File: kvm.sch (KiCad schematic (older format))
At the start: 35 parts, among them J1 USB_C_Receptacle, J2 Conn_ARM_JTAG_SWD_10, J3 USB_C_Receptacle, J4 USB_C_Receptacle, SW1 SW_Push, U1 MAX17501AxTB, U2 HD3SS3212, U3 HD3SS3212, U4 HD3SS3212, U5 STM32F030F4Px, U6 TS3A5223RSW, U7 UCS3205, U8 TS3A5223RSW, U9 UCS3205, Y1 16MHz

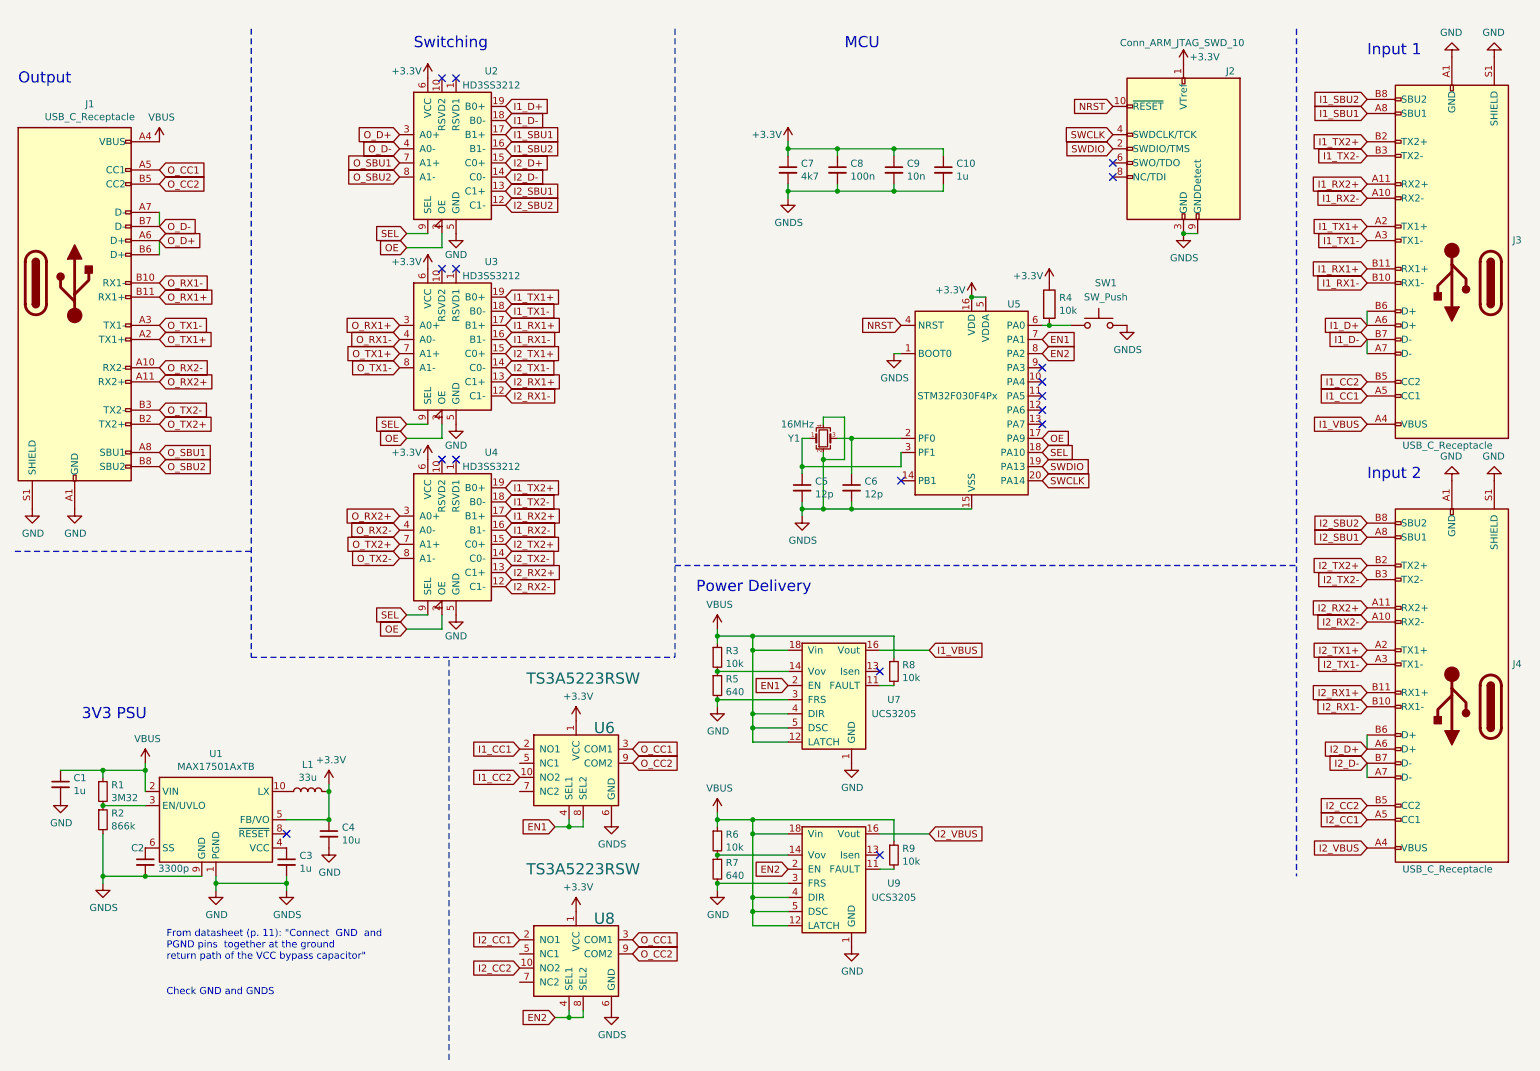
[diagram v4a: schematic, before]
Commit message: Fixed errors in component schematics and added decoupling caps
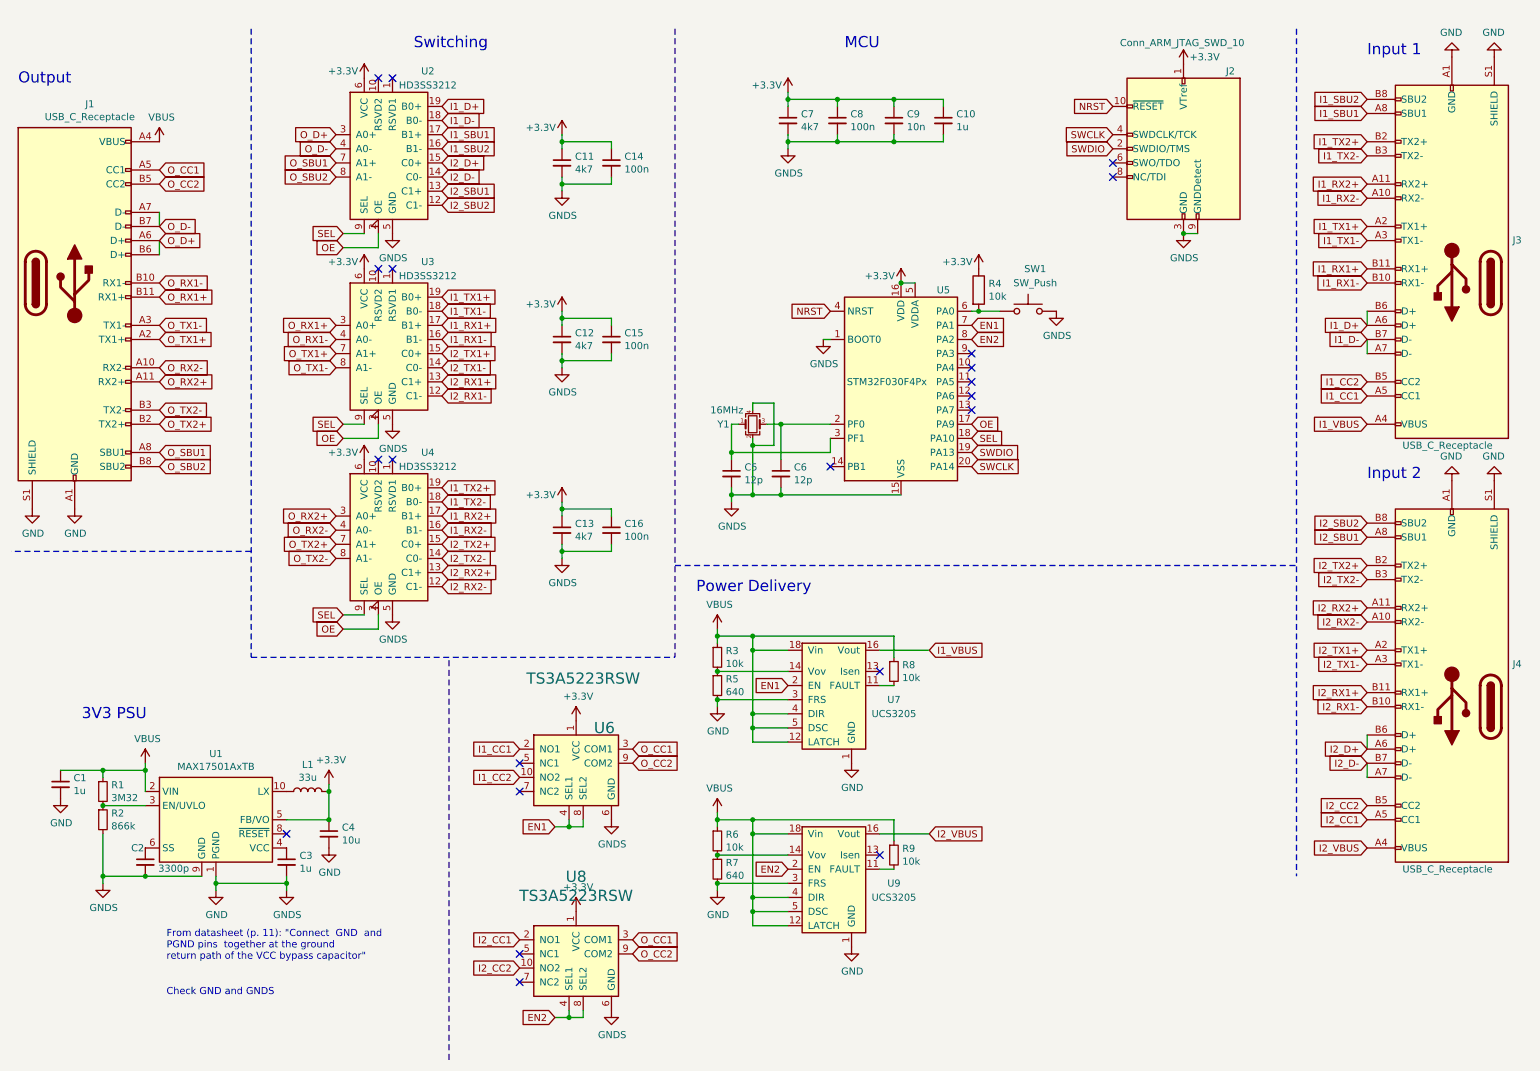
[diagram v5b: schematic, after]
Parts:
- added C11, C12, C13: 4k7, Capacitor_SMD:C_0402_1005Metric, symbol Device:C_Small
- added C14, C15, C16: 100n, Capacitor_SMD:C_0402_1005Metric, symbol Device:C_Small
- C1, C2, C3, C4: footprint (none) -> Capacitor_SMD:C_1206_3216Metric
- C10, C5, C6, C7, C8, C9: footprint (none) -> Capacitor_SMD:C_0402_1005Metric
- R1, R2, R3, R5, R6, R7, R8, R9: footprint (none) -> Resistor_SMD:R_1206_3216Metric
- R4: footprint Resistor_SMD:R_0805_2012Metric -> Resistor_SMD:R_0402_1005Metric
- U6, U8: footprint (none) -> VQFN20:VQFN19_3x3x0.9mm
- Y1: footprint (none) -> Crystal:Crystal_SMD_SeikoEpson_TSX3225-4Pin_3.2x2.5mm
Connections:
- net +3V3: now also C11.1, C12.1, C13.1, C14.1, C15.1, C16.1
- net GND: now also C11.2, C12.2, C13.2, C14.2, C15.2, C16.2
- no-connect marks 17 -> 21
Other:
- moved on the sheet: C10, C5, C6, C7, C8, C9, R4, SW1, U2, U3, U4, U5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

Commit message: Added separate power input for control circuit
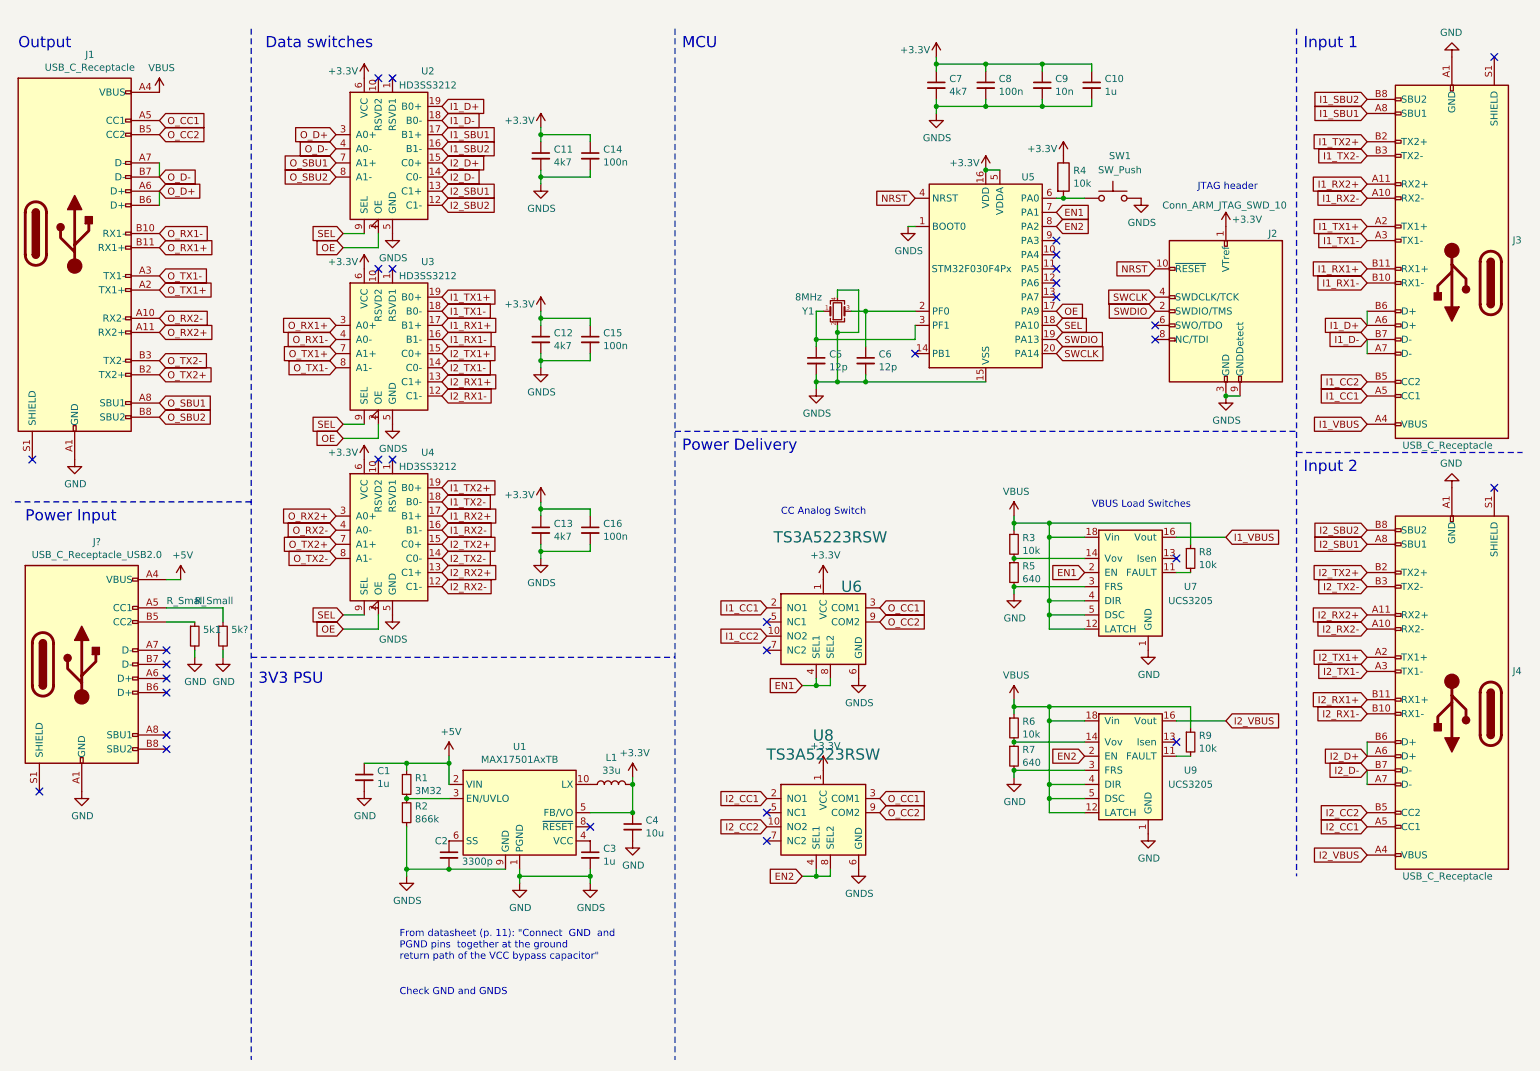
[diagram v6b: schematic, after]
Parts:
- added 5k1, 5k?: R_Small, symbol Device:R_Small
- added J?: USB_C_Receptacle_USB2.0, symbol Connector:USB_C_Receptacle_USB2.0
- Y1: value 16MHz -> 8MHz
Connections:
- net GND: now also 5k1.2, 5k?.2, J?.A1 (GND), J?.A12 (GND), J?.B1 (GND), J?.B12 (GND); no longer J1.S1 (SHIELD), J3.S1 (SHIELD), J4.S1 (SHIELD)
- net VBUS: no longer C1.1, R1.1, U1.2 (VIN)
- new net: 5k?.1, J?.A5 (CC1)
- new net: 5k1.1, J?.B5 (CC2)
- new net +5V: C1.1, J?.A4 (VBUS), J?.A9 (VBUS), J?.B4 (VBUS), J?.B9 (VBUS), R1.1, U1.2 (VIN)
- no-connect marks 21 -> 31
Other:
- note added: "CC Analog Switch"
- note added: "Data switches"
- note added: "JTAG header"
- note added: "Power Input"
- note added: "VBUS Load Switches"
- note removed: "Switching"
- moved on the sheet: C1, C10, C11, C12, C13, C14, C15, C16, C2, C3, C4, C5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

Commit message: Added annotations
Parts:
- gave numbers to parts that had none: 2
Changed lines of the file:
@@
 	5200 3350 9600 3350
 $Comp
-L Connector:USB_C_Receptacle_USB2.0 J?
+L Connector:USB_C_Receptacle_USB2.0 J5
 U 1 1 6179F699
 P 1000 5000
-F 0 "J?" H 1107 5867 50  0000 C CNN
+F 0 "J5" H 1107 5867 50  0000 C CNN
 F 1 "USB_C_Receptacle_USB2.0" H 1107 5776 50  0000 C CNN
 F 2 "" H 1150 5000 50  0001 C CNN
@@
 $EndComp
 $Comp
-L power:+5V #PWR?
+L power:+5V #PWR04
 U 1 1 617AE3D6
 P 1700 4400
-F 0 "#PWR?" H 1700 4250 50  0001 C CNN
+F 0 "#PWR04" H 1700 4250 50  0001 C CNN
 F 1 "+5V" H 1715 4573 50  0000 C CNN
 F 2 "" H 1700 4400 50  0001 C CNN
@@
 	1700 4400 1600 4400
 $Comp
-L power:+5V #PWR?
+L power:+5V #PWR043
 U 1 1 617BB74B
 P 3600 5650
-F 0 "#PWR?" H 3600 5500 50  0001 C CNN
+F 0 "#PWR043" H 3600 5500 50  0001 C CNN
 F 1 "+5V" H 3615 5823 50  0000 C CNN
 F 2 "" H 3600 5650 50  0001 C CNN
@@
 $EndComp
 $Comp
-L power:GND #PWR?
+L power:GND #PWR01
 U 1 1 617CC1E5
 P 1000 5900
-F 0 "#PWR?" H 1000 5650 50  0001 C CNN
+F 0 "#PWR01" H 1000 5650 50  0001 C CNN
 F 1 "GND" H 1005 5727 50  0000 C CNN
 F 2 "" H 1000 5900 50  0001 C CNN
@@
 Power Input
 $Comp
-L power:GND #PWR?
+L power:GND #PWR032
 U 1 1 618A9089
 P 1800 4950
-F 0 "#PWR?" H 1800 4700 50  0001 C CNN
+F 0 "#PWR032" H 1800 4700 50  0001 C CNN
 F 1 "GND" H 1805 4777 50  0000 C CNN
 F 2 "" H 1800 4950 50  0001 C CNN
@@
 $EndComp
 $Comp
-L power:GND #PWR?
+L power:GND #PWR033
 U 1 1 618A9AEB
 P 2000 4950
-F 0 "#PWR?" H 2000 4700 50  0001 C CNN
+F 0 "#PWR033" H 2000 4700 50  0001 C CNN
 F 1 "GND" H 2005 4777 50  0000 C CNN
 F 2 "" H 2000 4950 50  0001 C CNN
@@
 	2000 4600 2000 4700
 $Comp
-L Device:R_Small 5k?
+L Device:R_Small 5k2
 U 1 1 61928C3F
 P 2000 4800
-F 0 "5k?" H 2059 4846 50  0000 L CNN
+F 0 "5k2" H 2059 4846 50  0000 L CNN
 F 1 "R_Small" H 1800 5050 50  0000 L CNN
 F 2 "" H 2000 4800 50  0001 C CNN
